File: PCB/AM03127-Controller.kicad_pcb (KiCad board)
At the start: 2 copper layers, 23 x 76 mm, 13 parts, among them U1 XIAO-ESP32-C3-DIP, U2 MAX3232, U3 AMS1117

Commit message: Refactor PCB to use global label  nets
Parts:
- DC1: renamed from 12V; value (none) -> DC050-T
- U3: value AMS1117 -> AMS1117 5.0
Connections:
- net /12V renamed +12V
- net /3.3V renamed +3.3V
- net /5V renamed Net-(C2-Pad1)
- net /5VD renamed +5V
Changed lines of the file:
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@@
 	(net 6 "Net-(U2-VS+)")
 	(net 7 "Net-(U2-VS-)")
-	(net 8 "/12V")
-	(net 9 "/5V")
-	(net 10 "/3.3V")
+	(net 8 "+12V")
+	(net 9 "Net-(C2-Pad1)")
+	(net 10 "+3.3V")
 	(net 11 "/RS232 TX")
 	(net 12 "unconnected-(U2-T2IN-Pad10)")
@@
 	(net 36 "unconnected-(U1-GPIO5{slash}A3{slash}D3-Pad4)_1")
 	(net 37 "unconnected-(U1-GPIO10{slash}D10{slash}MOSI-Pad11)_1")
-	(net 38 "/5VD")
+	(net 38 "+5V")
 	(footprint "RJ11:RJ11-TH_PCB-6P4C-90_C189746"
 		(layer "F.Cu")
@@
 			)
 		)
-		(property "Value" "AMS1117"
+		(property "Value" "AMS1117 5.0"
 			(at 0 5.4 90)
 			(layer "F.Fab")
@@
 			(layers "F.Cu" "F.Mask" "F.Paste")
 			(roundrect_rratio 0.2380952381)
-			(net 9 "/5V")
+			(net 9 "Net-(C2-Pad1)")
 			(pinfunction "VOUT")
 			(pintype "unspecified")
@@
 			(layers "F.Cu" "F.Mask" "F.Paste")
 			(roundrect_rratio 0.2380952381)
-			(net 8 "/12V")
+			(net 8 "+12V")
 			(pinfunction "VIN")
 			(pintype "unspecified")
@@
 			(layers "*.Cu" "F.Mask")
 			(remove_unused_layers no)
-			(net 9 "/5V")
+			(net 9 "Net-(C2-Pad1)")
 			(pinfunction "VOUT")
 			(pintype "unspecified")
@@
 			(layers "*.Cu" "F.Mask")
 			(remove_unused_layers no)
-			(net 9 "/5V")
+			(net 9 "Net-(C2-Pad1)")
 			(pinfunction "VOUT")
 			(pintype "unspecified")
@@
 			(layers "F.Cu" "F.Mask" "F.Paste")
 			(roundrect_rratio 0.1016260163)
-			(net 9 "/5V")
+			(net 9 "Net-(C2-Pad1)")
 			(pinfunction "VOUT")
 			(pintype "unspecified")
@@
 			(layers "B.Cu")
 			(roundrect_rratio 0.1016260163)
-			(net 9 "/5V")
+			(net 9 "Net-(C2-Pad1)")
 			(pinfunction "VOUT")
 			(pintype "unspecified")
@@
 			(layers "*.Cu" "F.Mask")
 			(remove_unused_layers no)
-			(net 9 "/5V")
+			(net 9 "Net-(C2-Pad1)")
 			(pinfunction "VOUT")
 			(pintype "unspecified")
@@
 		(layer "F.Cu")
 		(at 135.4 135.5 -90)
-		(property "Reference" "12V"
+		(property "Reference" "DC1"
 			(at 5.75 -8.6 0)
 			(layer "F.SilkS")
@@
 			)
 		)
-		(property "Value" ""
+		(property "Value" "DC050-T"
 			(at 0.75 -9.35 90)
 			(layer "F.Fab")
@@
 			(size 2 2.1)
 			(layers "F.Cu" "F.Mask" "F.Paste")
-			(net 8 "/12V")
+			(net 8 "+12V")
 			(pinfunction "1")
 			(pintype "unspecified")
@@
 			(size 2 2.1)
 			(layers "F.Cu" "F.Mask" "F.Paste")
-			(net 8 "/12V")
+			(net 8 "+12V")
 			(pinfunction "1")
 			(pintype "unspecified")
@@
 			(net 15 "unconnected-(U2-T2OUT-Pad7)")
 			(pinfunction "T2OUT")
-			(pintype "output")
+			(pintype "output+no_connect")
 		)
 		(pad "8" smd roundrect
@@
 			(layers "F.Cu" "F.Mask" "F.Paste")
 			(roundrect_rratio 0.25)
-			(net 10 "/3.3V")
+			(net 10 "+3.3V")
 			(pinfunction "VCC")
 			(pintype "power_in")
@@
 			(layers "F.Cu" "F.Mask" "F.Paste")
 			(roundrect_rratio 0.217391)
-			(net 8 "/12V")
+			(net 8 "+12V")
 			(pintype "passive")
 		)
@@
 			(layers "F.Cu" "F.Mask" "F.Paste")
 			(roundrect_rratio 0.25)
-			(net 38 "/5VD")
+			(net 38 "+5V")
 			(pintype "passive")
 		)
@@
 			(layers "F.Cu" "F.Mask" "F.Paste")
 			(roundrect_rratio 0.25)
-			(net 9 "/5V")
+			(net 9 "Net-(C2-Pad1)")
 			(pintype "passive")
 		)
@@
 			(layers "F.Cu" "F.Mask" "F.Paste")
 			(roundrect_rratio 0.217391)
-			(net 9 "/5V")
+			(net 9 "Net-(C2-Pad1)")
 			(pintype "passive")
 		)
@@
 			(layers "F.Cu" "F.Mask" "F.Paste")
 			(roundrect_rratio 0.25)
-			(net 10 "/3.3V")
+			(net 10 "+3.3V")
 			(pintype "passive")
 		)
@@
 			(layers "*.Cu" "*.Mask")
 			(remove_unused_layers no)
-			(net 10 "/3.3V")
+			(net 10 "+3.3V")
 			(pinfunction "VCC_3V3")
 			(pintype "passive")
@@
 			(layers "F.Cu" "F.Mask")
 			(roundrect_rratio 0.1)
-			(net 10 "/3.3V")
+			(net 10 "+3.3V")
 			(pinfunction "VCC_3V3")
 			(pintype "passive")
@@
 			(layers "*.Cu" "*.Mask")
 			(remove_unused_layers no)
-			(net 38 "/5VD")
+			(net 38 "+5V")
 			(pinfunction "VBUS")
 			(pintype "passive")
@@
 			(layers "F.Cu" "F.Mask")
 			(roundrect_rratio 0.1)
-			(net 38 "/5VD")
+			(net 38 "+5V")
 			(pinfunction "VBUS")
 			(pintype "passive")

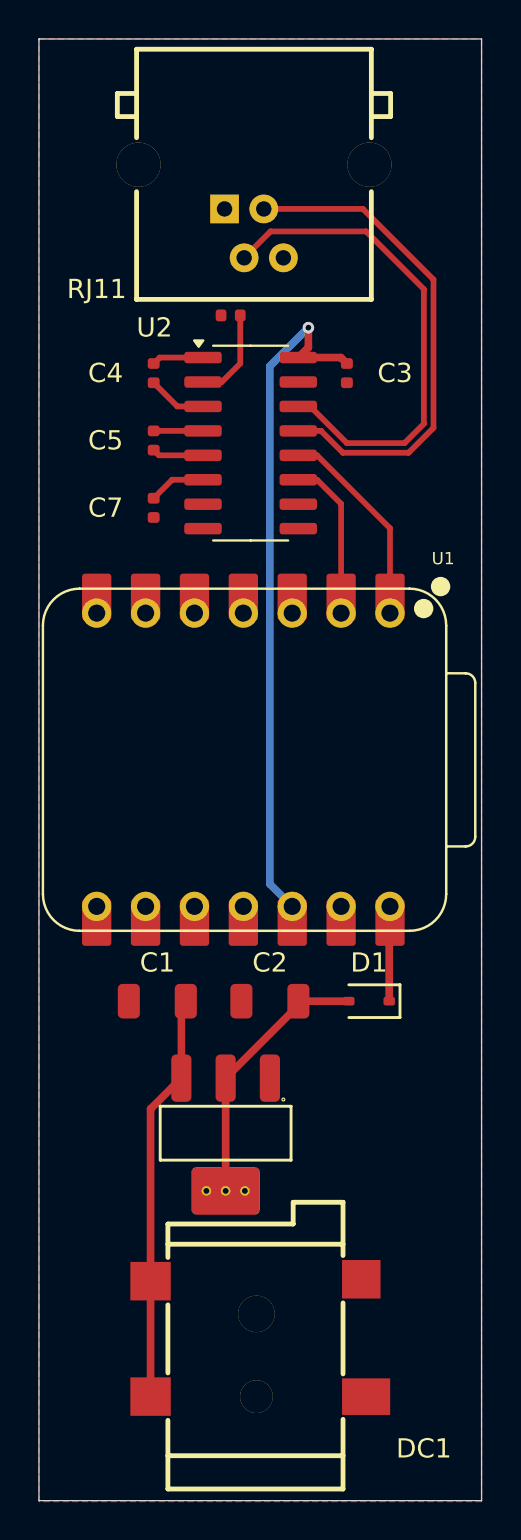
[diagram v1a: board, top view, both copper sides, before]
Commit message: Refactor LDO to Buckconverter
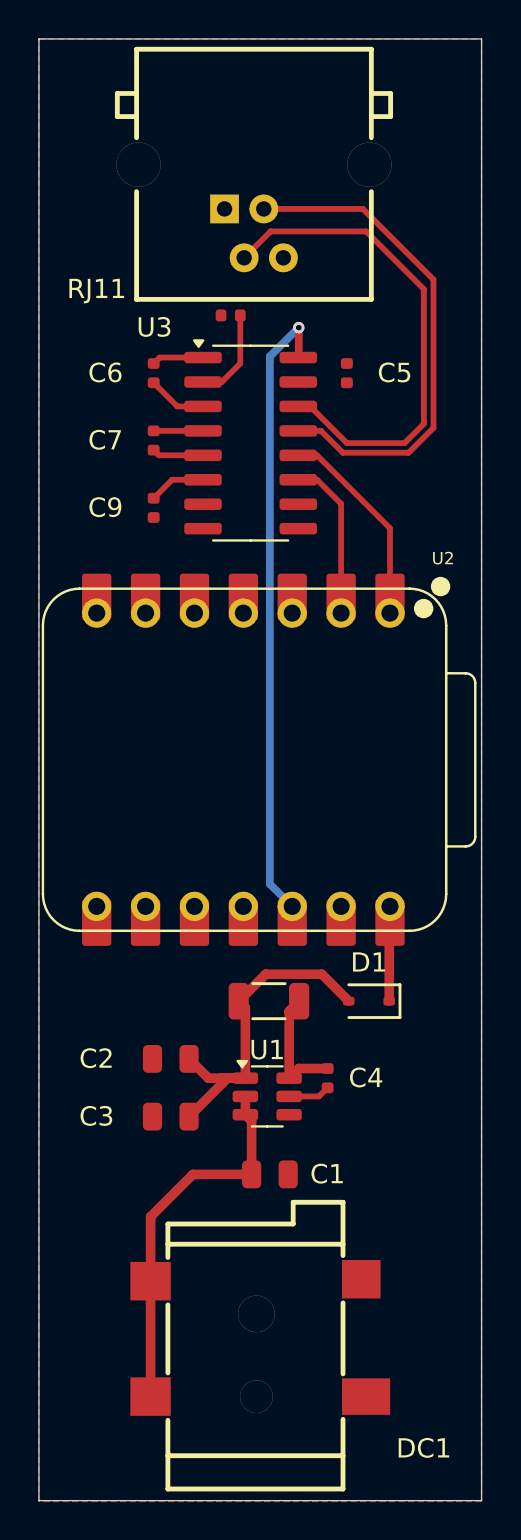
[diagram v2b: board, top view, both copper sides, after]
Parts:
- removed the U3 at (133.7, 124.9)
- added C3: 22uF, PCM_JLCPCB:C_0805, F.Cu at (130.8, 124.0)
- added C4: 100nF, PCM_JLCPCB:C_0402, F.Cu at (139.0, 122.0)
- added L1: 10uH,25mA, PCM_JLCPCB:L_1206, F.Cu at (135.9, 118.0)
- added U1: AP63205WU, Package_TO_SOT_SMD:TSOT-23-6, F.Cu at (135.9, 123.0)
- C1, C2: footprint PCM_JLCPCB:C_1206 -> PCM_JLCPCB:C_0805
- moved C1 10.7 mm to (136.0, 127.0), turned to 0 degrees
- moved C2 5.96 mm to (130.8, 121.0)
- renumbered C3 to C5, C4 to C6, C5 to C7, C6 to C8, C7 to C9, U1 to U2, U2 to U3
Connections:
- net Net-(C2-Pad1) renamed /BuckFeedback
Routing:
- net /BuckOut: track 0.00 -> 6.42 mm
- net /BuckFeedback: track 14.0 -> 19.4 mm
- net +3.3V: track 36.6 -> 33.6 mm
- net Net-(U1-SW): track 0.00 -> 2.19 mm
- net +12V: track 21.3 -> 19.7 mm
- net /UART RX: track 12.6 -> 11.6 mm
